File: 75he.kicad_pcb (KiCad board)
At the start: 2 copper layers, 317.6 x 131.8 mm, 391 parts, among them J201 Connector, USB-TYPE-C-16P, K1 DRV5055A3xDBZxQ1, K10 DRV5055A3xDBZxQ1, K11 DRV5055A3xDBZxQ1, K12 DRV5055A3xDBZxQ1, K13 DRV5055A3xDBZxQ1, K14 DRV5055A3xDBZxQ1, K15 DRV5055A3xDBZxQ1, K16 DRV5055A3xDBZxQ1, K17 DRV5055A3xDBZxQ1, K18 DRV5055A3xDBZxQ1, K19 DRV5055A3xDBZxQ1, K2 DRV5055A3xDBZxQ1, K20 DRV5055A3xDBZxQ1, K21 DRV5055A3xDBZxQ1, K22 DRV5055A3xDBZxQ1, K23 DRV5055A3xDBZxQ1, K24 DRV5055A3xDBZxQ1, K25 DRV5055A3xDBZxQ1, K26 DRV5055A3xDBZxQ1, K27 DRV5055A3xDBZxQ1, K28 DRV5055A3xDBZxQ1, K29 DRV5055A3xDBZxQ1, K3 DRV5055A3xDBZxQ1, K30 DRV5055A3xDBZxQ1, K31 DRV5055A3xDBZxQ1, K32 DRV5055A3xDBZxQ1, K33 DRV5055A3xDBZxQ1, K34 DRV5055A3xDBZxQ1, K35 DRV5055A3xDBZxQ1, K36 DRV5055A3xDBZxQ1, K37 DRV5055A3xDBZxQ1, K38 DRV5055A3xDBZxQ1, K39 DRV5055A3xDBZxQ1, K4 DRV5055A3xDBZxQ1, K40 DRV5055A3xDBZxQ1, K41 DRV5055A3xDBZxQ1, K42 DRV5055A3xDBZxQ1, K43 DRV5055A3xDBZxQ1, K44 DRV5055A3xDBZxQ1, K45 DRV5055A3xDBZxQ1, K46 DRV5055A3xDBZxQ1, K47 DRV5055A3xDBZxQ1, K48 DRV5055A3xDBZxQ1, K49 DRV5055A3xDBZxQ1, K5 DRV5055A3xDBZxQ1, K50 DRV5055A3xDBZxQ1, K51 DRV5055A3xDBZxQ1, K52 DRV5055A3xDBZxQ1, K53 DRV5055A3xDBZxQ1, K54 DRV5055A3xDBZxQ1, K55 DRV5055A3xDBZxQ1, K56 DRV5055A3xDBZxQ1, K57 DRV5055A3xDBZxQ1, K58 DRV5055A3xDBZxQ1, K59 DRV5055A3xDBZxQ1, K6 DRV5055A3xDBZxQ1, K60 DRV5055A3xDBZxQ1, K61 DRV5055A3xDBZxQ1, K62 DRV5055A3xDBZxQ1, K63 DRV5055A3xDBZxQ1, K64 DRV5055A3xDBZxQ1, K65 DRV5055A3xDBZxQ1, K66 DRV5055A3xDBZxQ1, K67 DRV5055A3xDBZxQ1, K68 DRV5055A3xDBZxQ1, K69 DRV5055A3xDBZxQ1, K7 DRV5055A3xDBZxQ1, K70 DRV5055A3xDBZxQ1, K71 DRV5055A3xDBZxQ1, K72 DRV5055A3xDBZxQ1, K73 DRV5055A3xDBZxQ1, K74 DRV5055A3xDBZxQ1, K75 DRV5055A3xDBZxQ1, K76 DRV5055A3xDBZxQ1, K77 DRV5055A3xDBZxQ1, K78 DRV5055A3xDBZxQ1, K79 DRV5055A3xDBZxQ1, K8 DRV5055A3xDBZxQ1, K80 DRV5055A3xDBZxQ1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

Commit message: finish sensor out capacitor
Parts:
- C158: moved to B.Cu
- moved C90 255.3 mm to (44.2, 97.8)
- moved C120 254.9 mm to (60.9, 116.9)
- moved C60 244.1 mm to (42.0, 78.7)
- moved C30 236.5 mm to (37.1, 59.7)
- moved C74 129.4 mm to (180.1, 78.7)
- moved C118 121.3 mm to (327.6, 97.8)
- moved C44 119.4 mm to (170.5, 59.7)
- moved C14 109.6 mm to (161.0, 35.9)
- moved C88 105.3 mm to (301.4, 88.3)
- moved C58 94.8 mm to (327.7, 59.7)
- moved C156 88.1 mm to (158.5, 135.9)
- moved C28 65.0 mm to (303.9, 35.9)
- moved C158 28.5 mm to (246.6, 135.9)
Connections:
- C156 pad 2: K78_OUT -> K76_OUT
- K76 pad 2: K78_OUT -> K76_OUT
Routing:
- net K59_OUT: track 0.00 -> 40.6 mm
- net K62_OUT: track 0.00 -> 27.3 mm
- net K74_OUT: track 0.00 -> 25.3 mm
- net K75_OUT: track 0.00 -> 21.7 mm
- net K60_OUT: track 0.00 -> 19.6 mm
- net K61_OUT: track 0.00 -> 8.71 mm
- net K73_OUT: track 0.00 -> 1.80 mm
- net K63_OUT: track 0.00 -> 1.72 mm

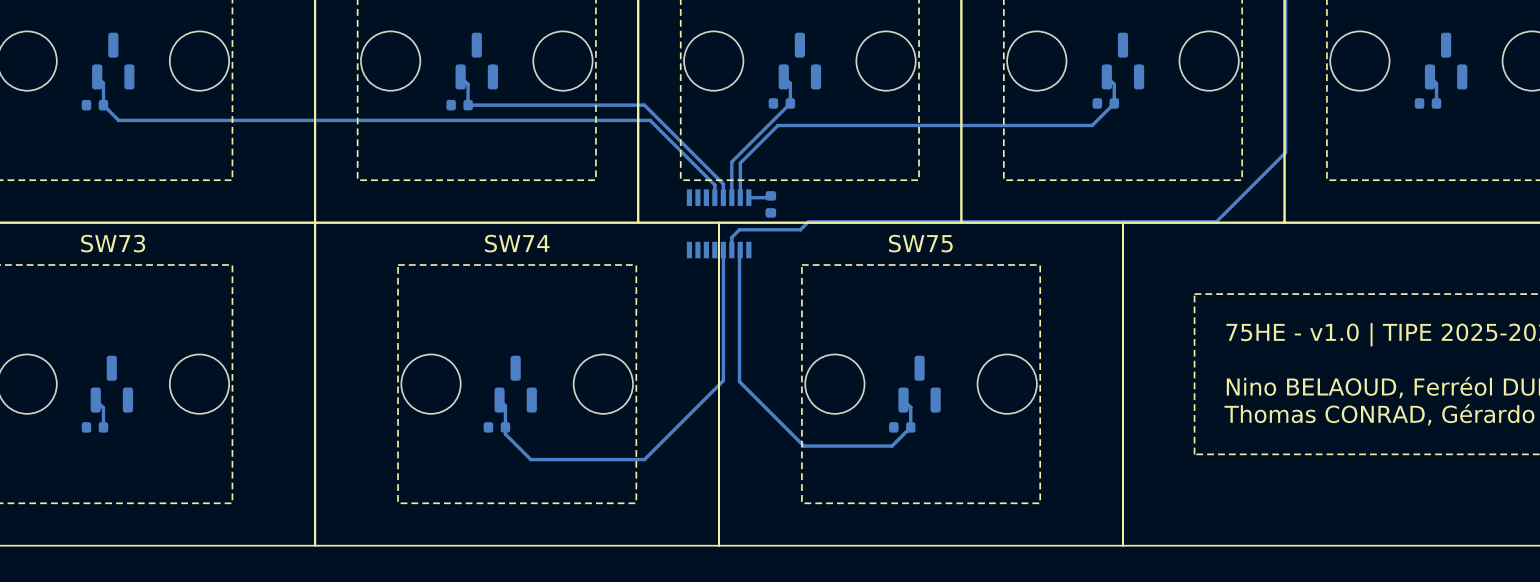
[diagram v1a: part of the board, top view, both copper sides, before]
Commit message: start sensor out routing
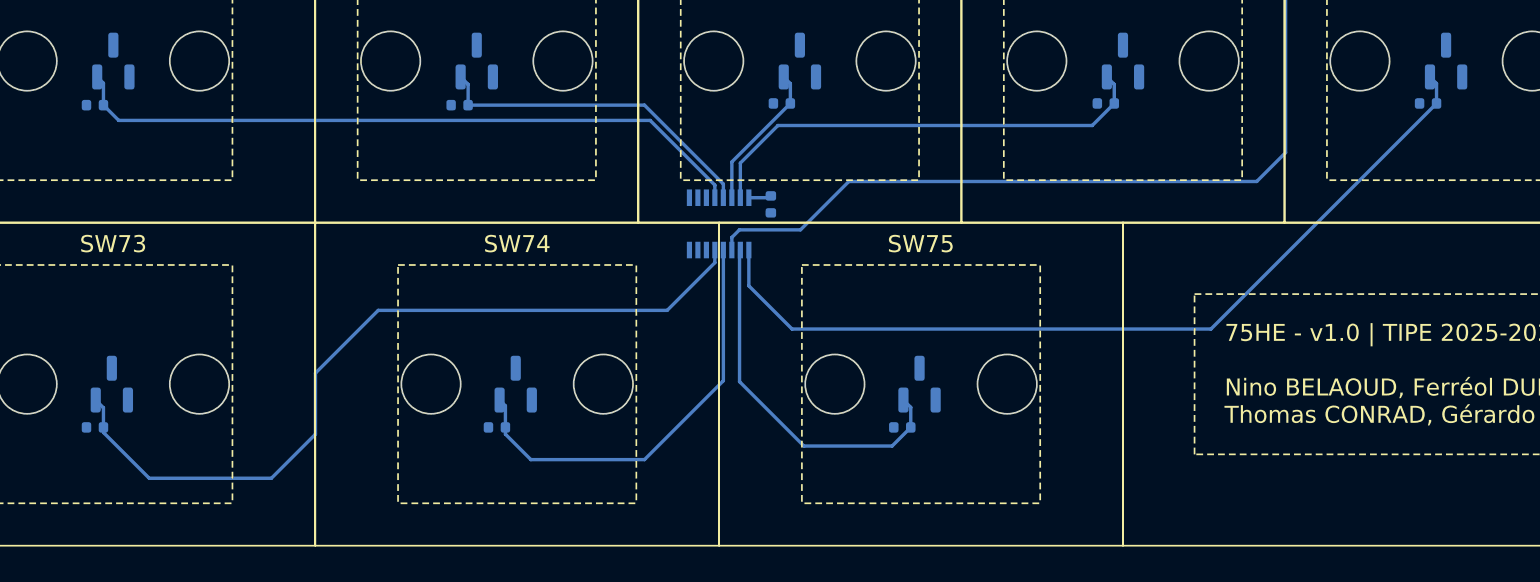
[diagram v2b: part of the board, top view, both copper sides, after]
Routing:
- net K63_OUT: track 1.72 -> 50.9 mm
- net K73_OUT: track 1.80 -> 47.4 mm
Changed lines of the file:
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@@
 	)
 	(segment
-		(start 105.525 123.775)
+		(start 109.6 119.7)
+		(end 109.6 107.5)
+		(width 0.2)
+		(layer "B.Cu")
+		(net 89)
+	)
+	(segment
+		(start 109.6 107.5)
+		(end 112.4 104.7)
+		(width 0.2)
+		(layer "B.Cu")
+		(net 89)
+	)
+	(segment
+		(start 77.400015 124.25)
+		(end 81 124.25)
+		(width 0.2)
+		(layer "B.Cu")
+		(net 89)
+	)
+	(segment
+		(start 131.2 55.8)
+		(end 134 53)
+		(width 0.2)
+		(layer "B.Cu")
+		(net 89)
+	)
+	(segment
+		(start 130.1 85.8)
+		(end 133.06 82.84)
+		(width 0.2)
+		(layer "B.Cu")
+		(net 89)
+	)
+	(segment
+		(start 107.9 121.4)
 		(end 109.6 119.7)
+		(width 0.2)
+		(layer "B.Cu")
+		(net 89)
+	)
+	(segment
+		(start 134 53)
+		(end 134 51.925)
+		(width 0.2)
+		(layer "B.Cu")
+		(net 89)
+	)
+	(segment
+		(start 115.5 104.7)
+		(end 119.1 101.1)
+		(width 0.2)
+		(layer "B.Cu")
+		(net 89)
+	)
+	(segment
+		(start 120.5 85.8)
+		(end 130.1 85.8)
+		(width 0.2)
+		(layer "B.Cu")
+		(net 89)
+	)
+	(segment
+		(start 119.1 87.2)
+		(end 120.5 85.8)
+		(width 0.2)
+		(layer "B.Cu")
+		(net 89)
+	)
+	(segment
+		(start 76.950189 125.44305)
+		(end 76.950189 124.699826)
 		(width 0.2)
 		(layer "B.Cu")
@@
 	)
 	(segment
-		(start 134 53)
-		(end 134 51.925)
+		(start 83.85 121.4)
+		(end 107.9 121.4)
+		(width 0.2)
+		(layer "B.Cu")
+		(net 89)
+	)
+	(segment
+		(start 112.4 104.7)
+		(end 115.5 104.7)
 		(width 0.2)
 		(layer "B.Cu")
@@
 	)
 	(segment
-		(start 112.4 104.7)
-		(end 115.5 104.7)
-		(width 0.2)
-		(layer "B.Cu")
-		(net 89)
-	)
-	(segment
 		(start 76.950189 124.699826)
 		(end 77.400015 124.25)
@@
 	)
 	(segment
-		(start 77.400015 124.25)
-		(end 81 124.25)
-		(width 0.2)
-		(layer "B.Cu")
-		(net 89)
-	)
-	(segment
-		(start 130.1 85.8)
-		(end 133.06 82.84)
-		(width 0.2)
-		(layer "B.Cu")
-		(net 89)
-	)
-	(segment
-		(start 81 124.25)
-		(end 81.475 123.775)
-		(width 0.2)
-		(layer "B.Cu")
-		(net 89)
-	)
-	(segment
-		(start 109.6 119.7)
-		(end 109.6 107.5)
-		(width 0.2)
-		(layer "B.Cu")
-		(net 89)
-	)
-	(segment
-		(start 109.6 107.5)
-		(end 112.4 104.7)
-		(width 0.2)
-		(layer "B.Cu")
-		(net 89)
-	)
-	(segment
-		(start 131.2 55.8)
-		(end 134 53)
-		(width 0.2)
-		(layer "B.Cu")
-		(net 89)
-	)
-	(segment
 		(start 131.2 62.6)
 		(end 131.2 55.8)
@@
 	)
 	(segment
-		(start 115.5 104.7)
-		(end 119.1 101.1)
-		(width 0.2)
-		(layer "B.Cu")
-		(net 89)
-	)
-	(segment
-		(start 76.950189 125.44305)
-		(end 76.950189 124.699826)
-		(width 0.2)
-		(layer "B.Cu")
-		(net 89)
-	)
-	(segment
-		(start 81.475 123.775)
-		(end 105.525 123.775)
-		(width 0.2)
-		(layer "B.Cu")
-		(net 89)
-	)
-	(segment
-		(start 120.5 85.8)
-		(end 130.1 85.8)
-		(width 0.2)
-		(layer "B.Cu")
-		(net 89)
-	)
-	(segment
-		(start 119.1 87.2)
-		(end 120.5 85.8)
+		(start 81 124.25)
+		(end 83.85 121.4)
 		(width 0.2)
 		(layer "B.Cu")
@@
 	)
 	(segment
+		(start 105.2 130.1)
+		(end 118.5 116.8)
+		(width 0.2)
+		(layer "B.Cu")
+		(net 205)
+	)
+	(segment
 		(start 118.5 115.625)
 		(end 118.1125 115.2375)
@@
 	)
 	(segment
+		(start 80.5 130.1)
+		(end 105.2 130.1)
+		(width 0.2)
+		(layer "B.Cu")
+		(net 205)
+	)
+	(segment
+		(start 77.950441 127.550441)
+		(end 80.5 130.1)
+		(width 0.2)
+		(layer "B.Cu")
+		(net 205)
+	)
+	(segment
 		(start 118.5 116.8)
 		(end 118.5 115.625)
@@
 	)
 	(segment
+		(start 77.950441 125.44305)
+		(end 77.950441 127.550441)
+		(width 0.2)
+		(layer "B.Cu")
+		(net 205)
+	)
+	(segment
+		(start 52.4 132.7)
+		(end 56.1 129)
+		(width 0.2)
+		(layer "B.Cu")
+		(net 213)
+	)
+	(segment
+		(start 56.1 129)
+		(end 73.136211 129)
+		(width 0.2)
+		(layer "B.Cu")
+		(net 213)
+	)
+	(segment
+		(start 75.949937 126.186274)
+		(end 75.949937 125.44305)
+		(width 0.2)
+		(layer "B.Cu")
+		(net 213)
+	)
+	(segment
+		(start 42.6 138.9)
+		(end 49.8 138.9)
+		(width 0.2)
+		(layer "B.Cu")
+		(net 213)
+	)
+	(segment
+		(start 39.9 136.2)
+		(end 42.6 138.9)
+		(width 0.2)
+		(layer "B.Cu")
+		(net 213)
+	)
+	(segment
+		(start 73.136211 129)
+		(end 75.949937 126.186274)
+		(width 0.2)
+		(layer "B.Cu")
+		(net 213)
+	)
+	(segment
 		(start 39.9 135.9)
 		(end 39.9 134.74375)
@@
 	)
 	(segment
+		(start 52.4 136.3)
+		(end 52.4 132.7)
+		(width 0.2)
+		(layer "B.Cu")
+		(net 213)
+	)
+	(segment
+		(start 39.9 135.9)
+		(end 39.9 136.2)
+		(width 0.2)
+		(layer "B.Cu")
+		(net 213)
+	)
+	(segment
 		(start 39.9 134.74375)
 		(end 39.44375 134.2875)
 		(width 0.2)
 		(layer "B.Cu")
+		(net 213)
+	)
+	(segment
+		(start 49.8 138.9)
+		(end 52.4 136.3)
+		(width 0.2)
+		(layer "B.Cu")

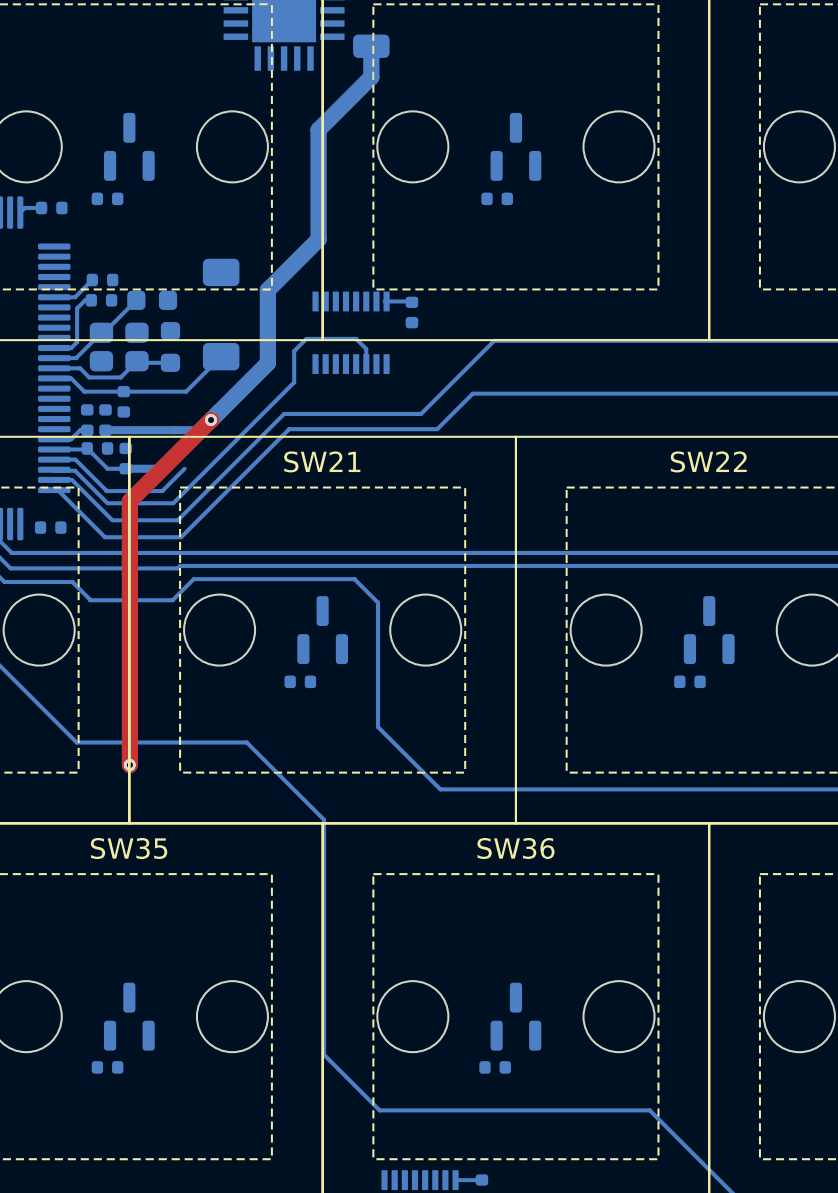
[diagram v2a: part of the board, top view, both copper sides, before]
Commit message: start sensor power rail
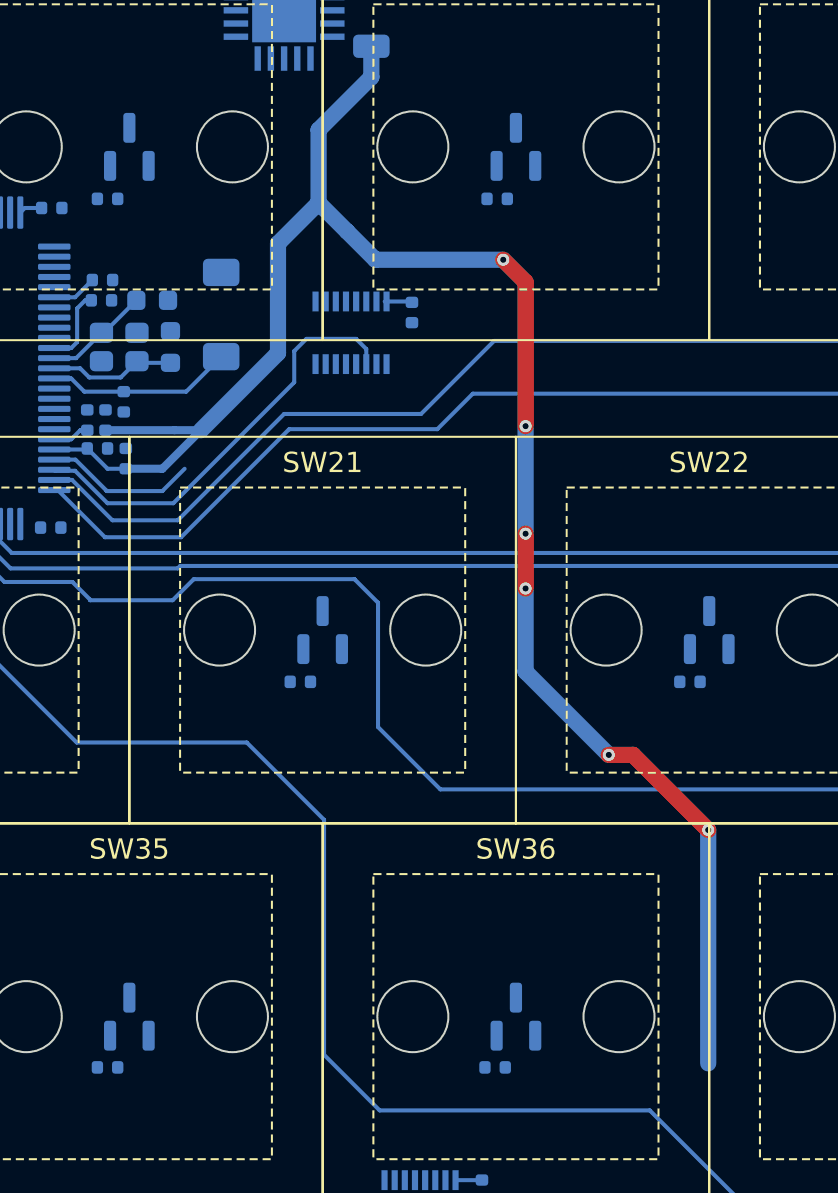
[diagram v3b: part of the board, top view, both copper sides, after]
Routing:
- net +3.3VA: track 70.5 -> 106.1 mm, vias 2 -> 6
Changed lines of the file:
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@@
 	)
 	(segment
-		(start 142.9 50.8)
-		(end 142.9 63.8)
-		(width 0.8)
-		(layer "F.Cu")
-		(net 102)
-	)
-	(segment
-		(start 146.9 46.8)
-		(end 142.9 50.8)
-		(width 0.8)
-		(layer "F.Cu")
-		(net 102)
-	)
-	(via
-		(at 146.9 46.8)
-		(size 0.6)
-		(drill 0.3)
-		(layers "F.Cu" "B.Cu")
-		(net 102)
-	)
-	(via
-		(at 142.9 63.8)
+		(start 167.7 63.3)
+		(end 171.4 67)
+		(width 0.8)
+		(layer "F.Cu")
+		(net 102)
+	)
+	(segment
+		(start 162.4 40)
+		(end 162.4 47.1)
+		(width 0.8)
+		(layer "F.Cu")
+		(net 102)
+	)
+	(segment
+		(start 166.5 63.3)
+		(end 167.7 63.3)
+		(width 0.8)
+		(layer "F.Cu")
+		(net 102)
+	)
+	(segment
+		(start 162.4 52.4)
+		(end 162.4 55.1)
+		(width 0.8)
+		(layer "F.Cu")
+		(net 102)
+	)
+	(segment
+		(start 161.3 38.9)
+		(end 162.4 40)
+		(width 0.8)
+		(layer "F.Cu")
+		(net 102)
+	)
+	(via
+		(at 166.5 63.3)
+		(size 0.6)
+		(drill 0.3)
+		(layers "F.Cu" "B.Cu")
+		(net 102)
+	)
+	(via
+		(at 162.4 47.1)
+		(size 0.6)
+		(drill 0.3)
+		(layers "F.Cu" "B.Cu")
+		(net 102)
+	)
+	(via
+		(at 171.4 67)
+		(size 0.6)
+		(drill 0.3)
+		(layers "F.Cu" "B.Cu")
+		(net 102)
+	)
+	(via
+		(at 161.3 38.9)
+		(size 0.6)
+		(drill 0.3)
+		(layers "F.Cu" "B.Cu")
+		(net 102)
+	)
+	(via
+		(at 162.4 55.1)
+		(size 0.6)
+		(drill 0.3)
+		(layers "F.Cu" "B.Cu")
+		(net 102)
+	)
+	(via
+		(at 162.4 52.4)
 		(size 0.6)
 		(drill 0.3)
@@
 		(end 156.75695 40.95695)
 		(width 0.2)
+		(layer "B.Cu")
+		(net 102)
+	)
+	(segment
+		(start 171.4 67)
+		(end 171.4 78.5)
+		(width 0.8)
+		(layer "B.Cu")
+		(net 102)
+	)
+	(segment
+		(start 152.2 32.5)
+		(end 152.2 36.1)
+		(width 0.8)
+		(layer "B.Cu")
+		(net 102)
+	)
+	(segment
+		(start 162.4 55.1)
+		(end 162.4 59.2)
+		(width 0.8)
 		(layer "B.Cu")
 		(net 102)
@@
 	)
 	(segment
+		(start 153.6 37.5)
+		(end 155 38.9)
+		(width 0.8)
+		(layer "B.Cu")
+		(net 102)
+	)
+	(segment
 		(start 158.950441 84.25695)
 		(end 160.24305 84.25695)
@@
 	)
 	(segment
-		(start 152.2 32.5)
-		(end 152.2 37.9)
-		(width 0.8)
-		(layer "B.Cu")
-		(net 102)
-	)
-	(segment
 		(start 70.9639 43.7139)
 		(end 71 43.75)
@@
 	)
 	(segment
-		(start 149.7 40.4)
-		(end 149.7 44)
-		(width 0.8)
-		(layer "B.Cu")
-		(net 102)
-	)
-	(segment
-		(start 152.2 37.9)
-		(end 149.7 40.4)
-		(width 0.8)
-		(layer "B.Cu")
-		(net 102)
-	)
-	(segment
 		(start 154.8 29.9)
 		(end 152.2 32.5)
+		(width 0.8)
+		(layer "B.Cu")
+		(net 102)
+	)
+	(segment
+		(start 150.2 43.5)
+		(end 146.4 47.3)
 		(width 0.8)
 		(layer "B.Cu")
@@
 	)
 	(segment
+		(start 150.2 38.1)
+		(end 150.2 43.5)
+		(width 0.8)
+		(layer "B.Cu")
+		(net 102)
+	)
+	(segment
 		(start 294.75 41)
 		(end 296 41)
@@
 	)
 	(segment
+		(start 152.2 36.1)
+		(end 153.6 37.5)
+		(width 0.8)
+		(layer "B.Cu")
+		(net 102)
+	)
+	(segment
 		(start 140.75 48.25)
 		(end 140.8 48.2)
@@
 		(end 79.25 122.25)
 		(width 0.2)
-		(layer "B.Cu")
-		(net 102)
-	)
-	(segment
-		(start 146.9 46.8)
-		(end 146.4 47.3)
-		(width 0.4)
-		(layer "B.Cu")
-		(net 102)
-	)
-	(segment
-		(start 147.25 46.45)
-		(end 146.9 46.8)
-		(width 0.4)
 		(layer "B.Cu")
 		(net 102)
@@
 	)
 	(segment
-		(start 146.911 46.789)
-		(end 146.9 46.8)
-		(width 0.8)
-		(layer "B.Cu")
-		(net 102)
-	)
-	(segment
 		(start 154.8 28.38)
 		(end 154.8 29.9)
@@
 	)
 	(segment
+		(start 152.2 36.1)
+		(end 150.2 38.1)
+		(width 0.8)
+		(layer "B.Cu")
+		(net 102)
+	)
+	(segment
 		(start 293.95695 84.45695)
 		(end 294 84.5)
@@
 	)
 	(segment
+		(start 162.4 59.2)
+		(end 166.5 63.3)
+		(width 0.8)
+		(layer "B.Cu")
+		(net 102)
+	)
+	(segment
 		(start 69.700126 43.7139)
 		(end 70.9639 43.7139)
@@
 	)
 	(segment
-		(start 147.25 46.45)
-		(end 146.911 46.789)
+		(start 155 38.9)
+		(end 161.3 38.9)
+		(width 0.8)
+		(layer "B.Cu")
+		(net 102)
+	)
+	(segment
+		(start 162.4 47.1)
+		(end 162.4 52.4)
 		(width 0.8)
 		(layer "B.Cu")
@@
 		(layer "B.Cu")
 		(net 102)
-	)
-	(segment
-		(start 149.7 44)
-		(end 147.25 46.45)
-		(width 0.8)
-		(layer "B.Cu")
-		(net 102)

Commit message: start sensor power rail
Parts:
- C162: moved to B.Cu
- moved C162 242.2 mm to (308.5, 140.7)
- moved C171 2.53 mm to (113.0, 47.7)
- moved C14 0.10 mm to (160.9, 35.9)
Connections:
- M1 pad 1: K19_OUT -> K22_OUT
- M1 pad 4: K22_OUT -> K19_OUT
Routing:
- net +3.3VA: track 106.1 -> 473.5 mm, vias 6 -> 8
- net K69_OUT: track 0.00 -> 71.0 mm
- net K82_OUT: track 0.00 -> 63.2 mm
- net K64_OUT: track 0.00 -> 62.8 mm, vias 0 -> 2
- net K78_OUT: track 0.00 -> 61.1 mm
- net K19_OUT: track 0.00 -> 55.9 mm, vias 0 -> 12
- net K70_OUT: track 0.00 -> 50.8 mm
- net K45_OUT: track 0.00 -> 45.0 mm
- net K65_OUT: track 0.00 -> 44.9 mm, vias 0 -> 2
- net K30_OUT: track 0.00 -> 43.5 mm
- net K76_OUT: track 0.00 -> 43.5 mm, vias 0 -> 2
- net K15_OUT: track 0.00 -> 42.7 mm
- net K79_OUT: track 0.00 -> 42.6 mm
- net K5_OUT: track 0.00 -> 42.1 mm, vias 0 -> 6
- net K77_OUT: track 0.00 -> 41.5 mm
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
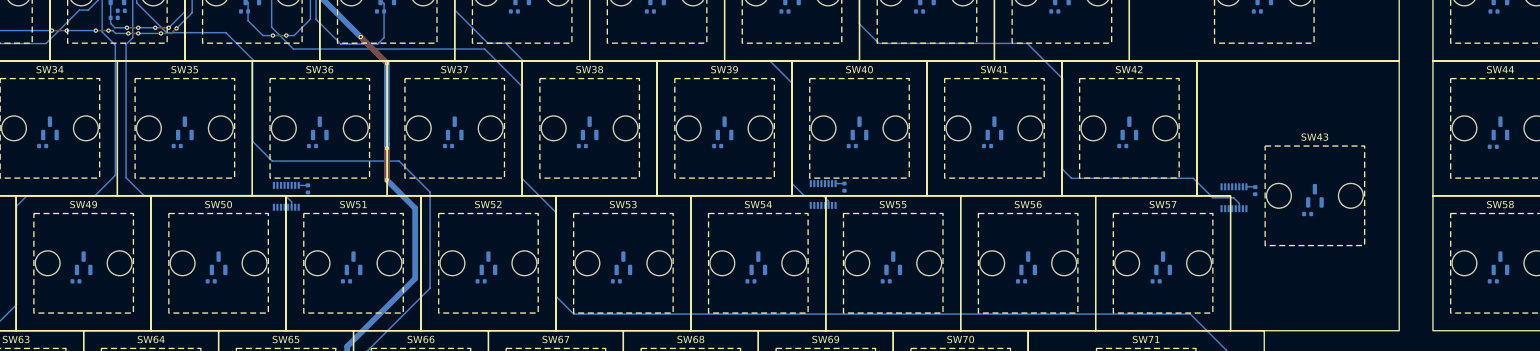
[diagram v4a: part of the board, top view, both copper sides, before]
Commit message: start sensor power rail
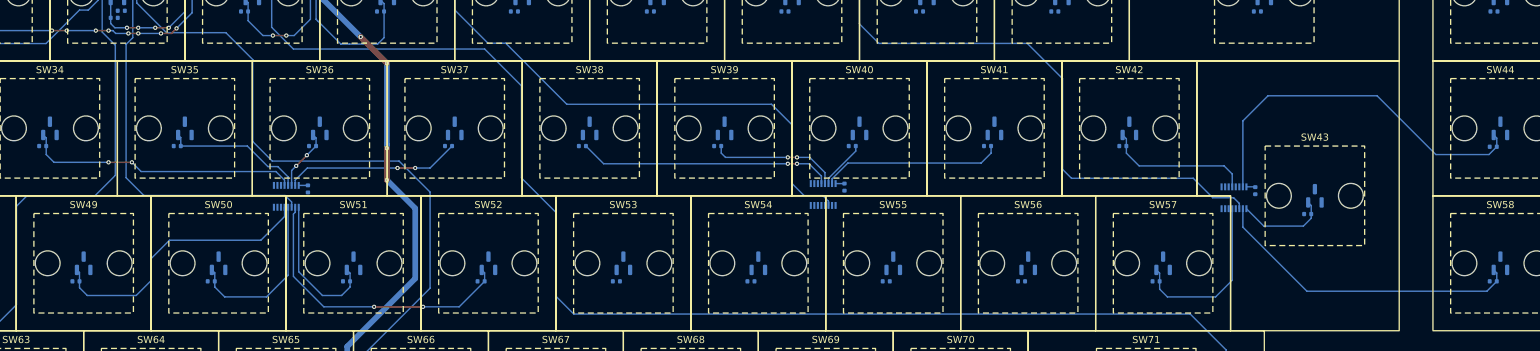
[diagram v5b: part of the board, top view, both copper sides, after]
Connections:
- M2 pad 12: unconnected-(M2-Y3-Pad12) -> K9_OUT
- M2 pad 13: unconnected-(M2-Y0-Pad13) -> K10_OUT
- M2 pad 14: unconnected-(M2-Y1-Pad14) -> K11_OUT
- M2 pad 15: unconnected-(M2-Y2-Pad15) -> K12_OUT
- M2 pad 2: unconnected-(M2-Y6-Pad2) -> K25_OUT
- M2 pad 4: unconnected-(M2-Y7-Pad4) -> K24_OUT
- M2 pad 5: unconnected-(M2-Y5-Pad5) -> K23_OUT
- M4 pad 1: unconnected-(M4-Y4-Pad1) -> K43_OUT
- M4 pad 12: unconnected-(M4-Y3-Pad12) -> K42_OUT
- M4 pad 15: unconnected-(M4-Y2-Pad15) -> K44_OUT
- M4 pad 2: unconnected-(M4-Y6-Pad2) -> K58_OUT
- M4 pad 5: unconnected-(M4-Y5-Pad5) -> K57_OUT
- M5 pad 1: unconnected-(M5-Y4-Pad1) -> K56_OUT
- M5 pad 12: unconnected-(M5-Y3-Pad12) -> K38_OUT
- M5 pad 13: unconnected-(M5-Y0-Pad13) -> K39_OUT
- M5 pad 14: unconnected-(M5-Y1-Pad14) -> K40_OUT
- M5 pad 15: unconnected-(M5-Y2-Pad15) -> K41_OUT
- M5 pad 2: unconnected-(M5-Y6-Pad2) -> K55_OUT
- M5 pad 4: unconnected-(M5-Y7-Pad4) -> K54_OUT
- M5 pad 5: unconnected-(M5-Y5-Pad5) -> K53_OUT
- M8 pad 1: K52_OUT -> K51_OUT
- M8 pad 14: K35_OUT -> K36_OUT
- M8 pad 15: K36_OUT -> K37_OUT
- M8 pad 2: K51_OUT -> K52_OUT
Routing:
- net K44_OUT: track 0.00 -> 52.4 mm
- net K58_OUT: track 0.00 -> 44.6 mm
- net K52_OUT: track 0.00 -> 41.9 mm, vias 0 -> 2
- net K49_OUT: track 0.00 -> 39.8 mm
- net K34_OUT: track 0.00 -> 38.8 mm, vias 0 -> 2
- net K38_OUT: track 0.00 -> 36.1 mm, vias 0 -> 2
- net K41_OUT: track 0.00 -> 25.6 mm
- net K37_OUT: track 0.00 -> 24.9 mm, vias 0 -> 2
- net K57_OUT: track 0.00 -> 24.7 mm
- net K50_OUT: track 0.00 -> 24.4 mm
- net K51_OUT: track 0.00 -> 20.8 mm
- net K42_OUT: track 0.00 -> 20.8 mm
- net K35_OUT: track 0.00 -> 19.9 mm
- net K39_OUT: track 0.00 -> 18.3 mm, vias 0 -> 2
- net K43_OUT: track 0.00 -> 13.0 mm
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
